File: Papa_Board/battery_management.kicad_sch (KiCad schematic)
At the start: 51 parts, among them J1 Conn_01x02_Female, J10 Conn_01x02_Female, J11 GND TEST CONN, J12 VOLTAGE TEST CONN, J7 Conn_01x02_Female, J9 Conn_01x02_Female, U1 INA180A4QDBVRQ1, U2 INA180A4QDBVRQ1, U3 LM22678TJ-5.0, U4 LDK320ADU120R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

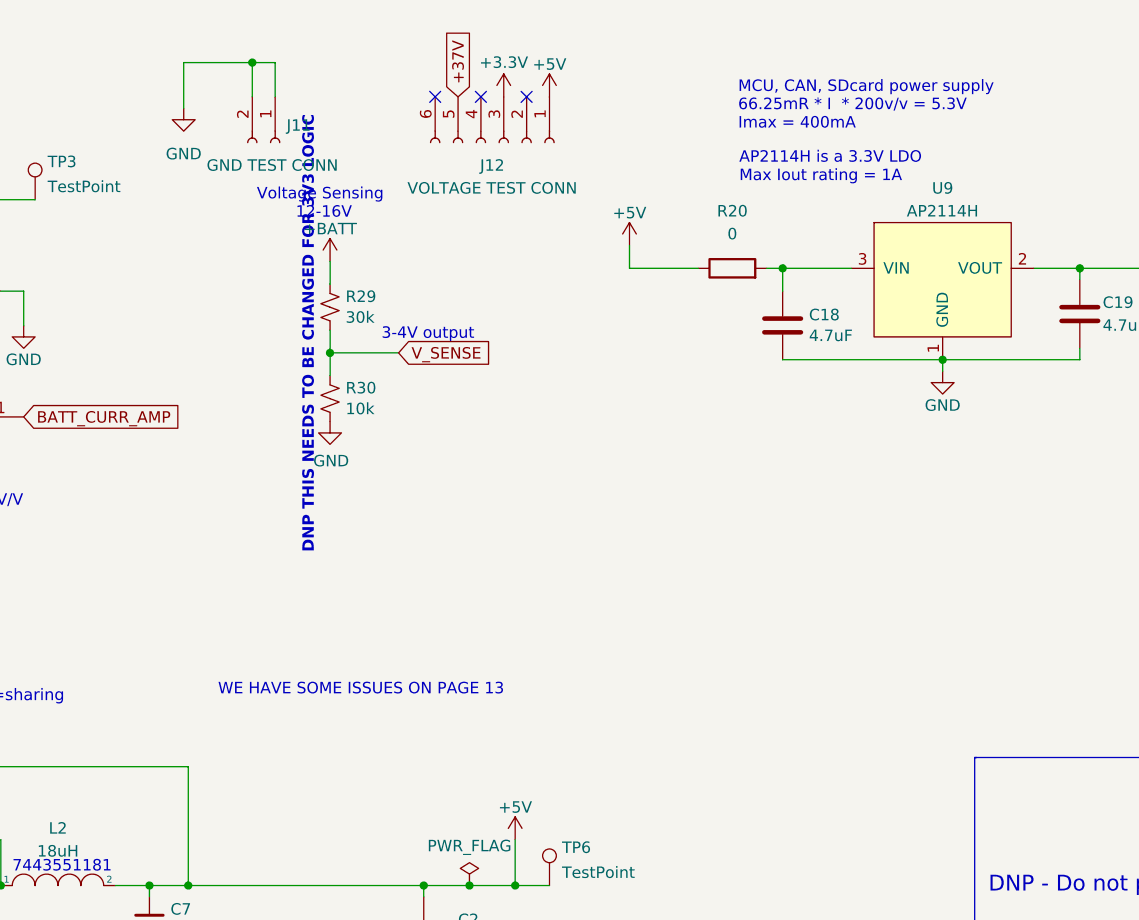
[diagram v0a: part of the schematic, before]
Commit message: Fix voltage sensing logic, finish lana's layout changes
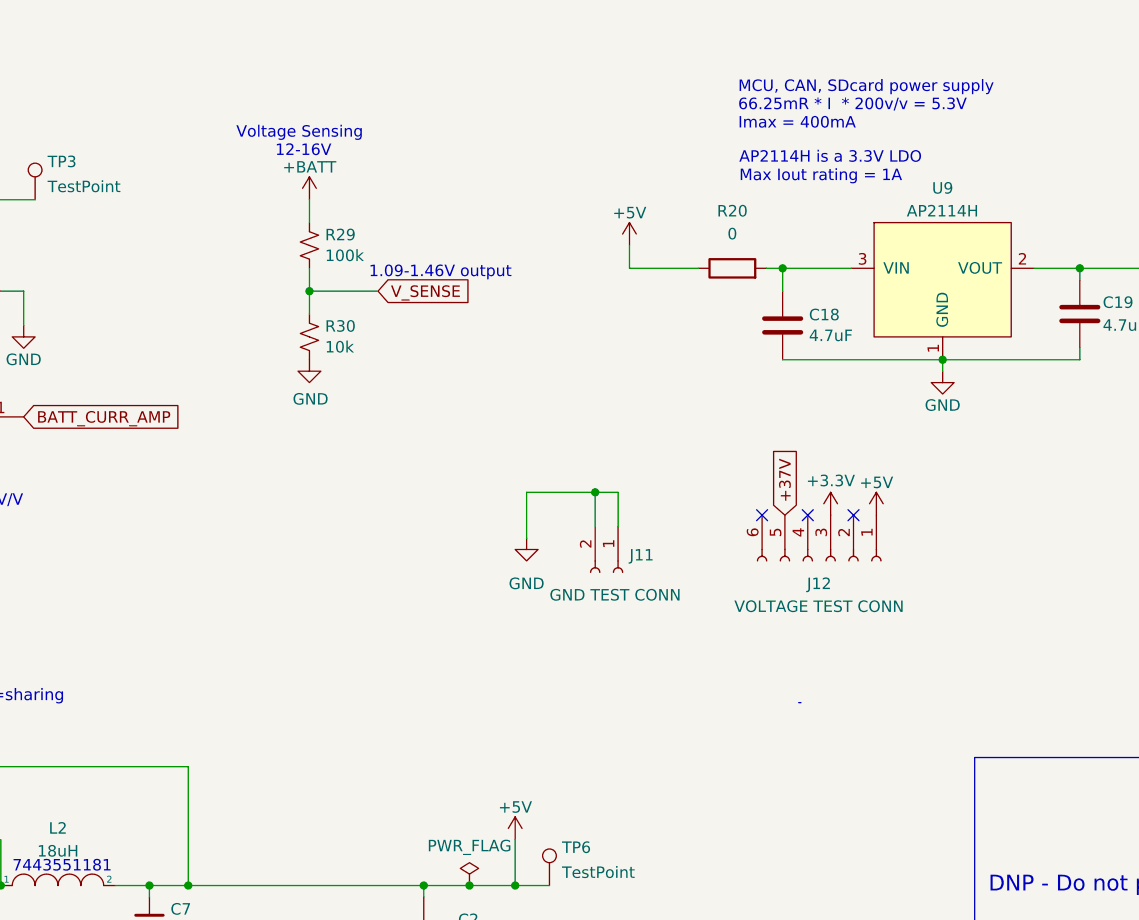
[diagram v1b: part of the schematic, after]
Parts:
- R29: value 30k -> 100k
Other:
- note added: "1.09-1.46V output"
- note removed: "3-4V output"
- note removed: "DNP THIS NEEDS TO BE CHANGED FOR 3V3 LOGIC"
- note removed: "WE HAVE SOME ISSUES ON PAGE 13"
- moved on the sheet: J11, J12, R29, R30

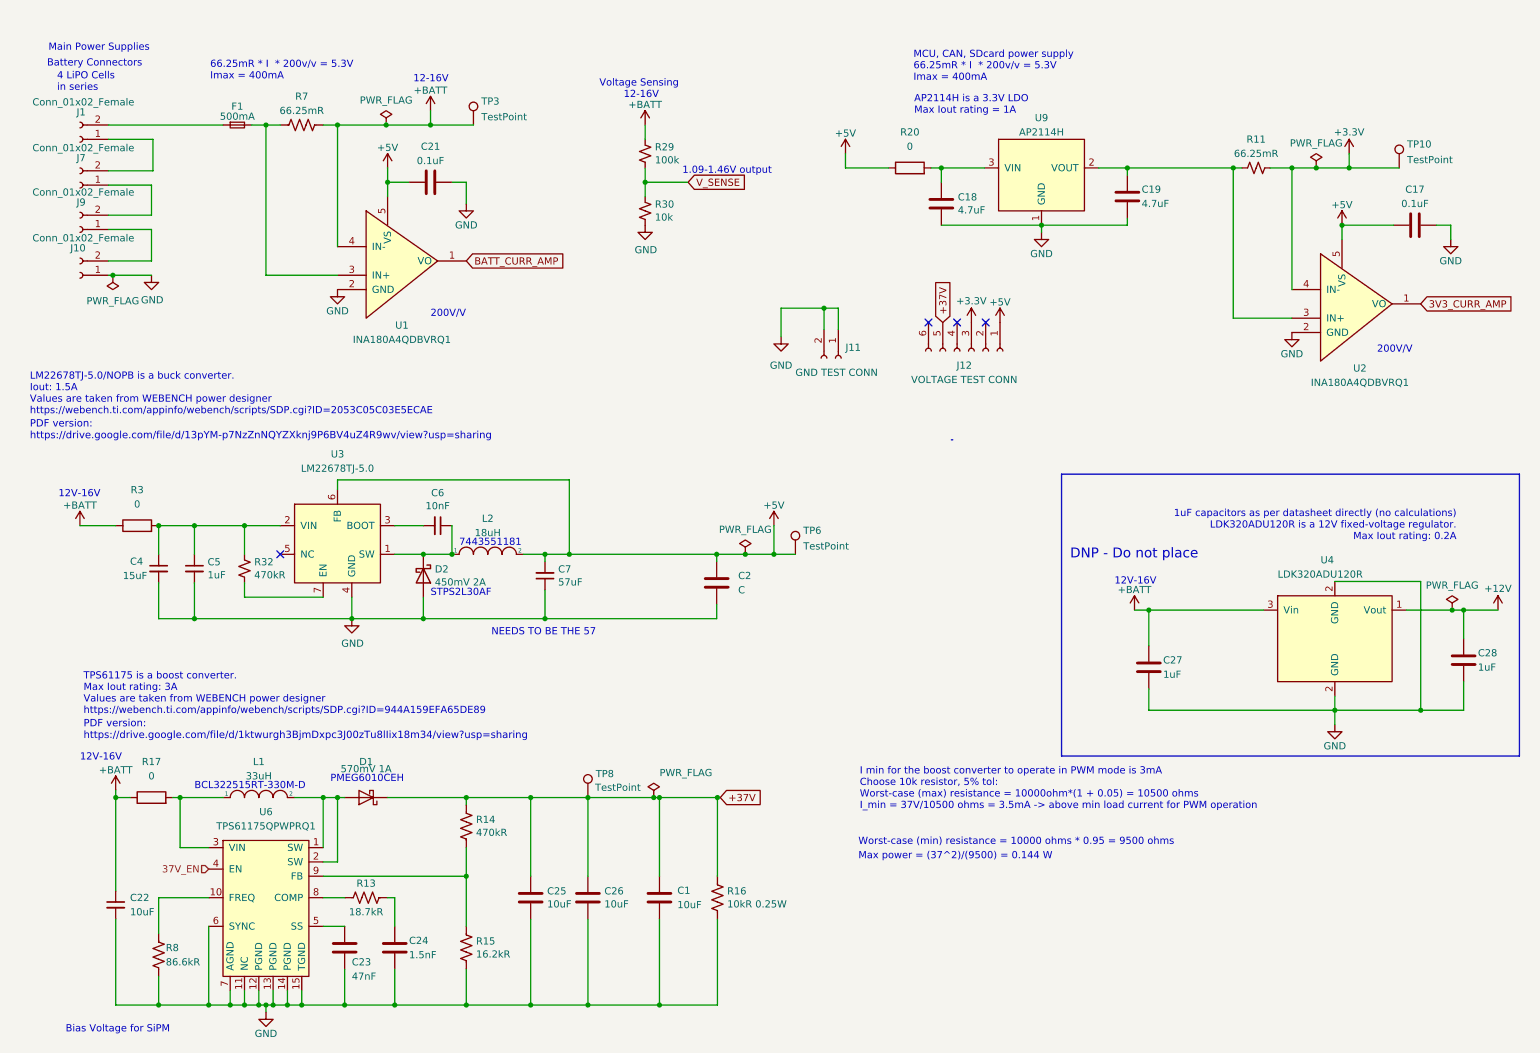
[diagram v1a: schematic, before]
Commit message: Address Jack's schematic review, still need to update PCB layout and figure out CAN connections
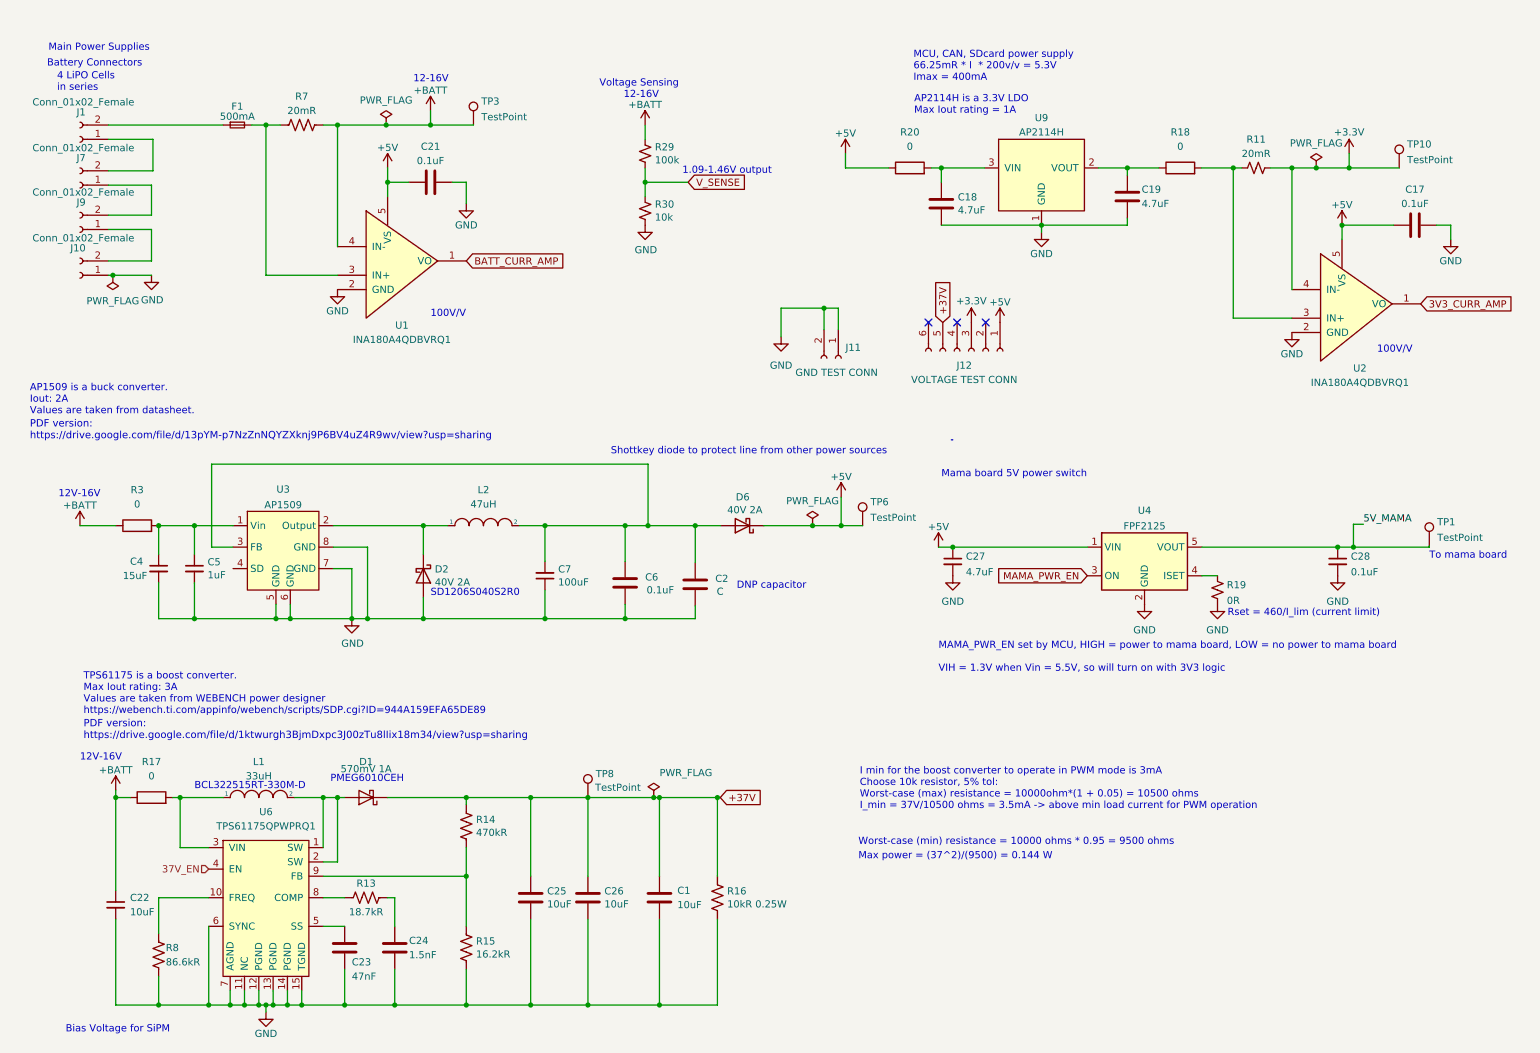
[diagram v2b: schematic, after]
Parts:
- removed C27, C28: 1uF, Capacitor_SMD:C_0805_2012Metric_Pad1.18x1.45mm_HandSolder, symbol Device:C
- removed C6: 10nF, Capacitor_SMD:C_0805_2012Metric_Pad1.18x1.45mm_HandSolder, symbol Device:C_Small
- removed R32: 470kR, Resistor_SMD:R_0805_2012Metric_Pad1.20x1.40mm_HandSolder, symbol Device:R_Small_US
- removed U3: LM22678TJ-5.0, Package_TO_SOT_SMD:TO-263-7_TabPin4, symbol payload2020_custom:LM22678TJ-5.0
- removed U4: LDK320ADU120R, Package_TO_SOT_SMD:SOT-89-3_Handsoldering, symbol payload2020_custom:LDK320ADU120R
- added C27: 4.7uF, Capacitor_SMD:C_0805_2012Metric_Pad1.18x1.45mm_HandSolder, symbol Device:C_Small
- added C28: 0.1uF, Capacitor_SMD:C_0805_2012Metric_Pad1.18x1.45mm_HandSolder, symbol Device:C_Small
- added C6: 0.1uF, Capacitor_SMD:C_0805_2012Metric_Pad1.18x1.45mm_HandSolder, symbol Device:C
- added D6: 40V 2A, Diode_SMD:D_1206_3216Metric_Pad1.42x1.75mm_HandSolder, symbol Device:D_Schottky
- added R18: 0, Resistor_SMD:R_0805_2012Metric_Pad1.20x1.40mm_HandSolder, symbol Device:R
- added R19: 0R, Resistor_SMD:R_0805_2012Metric_Pad1.20x1.40mm_HandSolder, symbol Device:R_Small_US
- added TP1: TestPoint, Connector_PinHeader_2.54mm:PinHeader_1x01_P2.54mm_Vertical, symbol Connector:TestPoint
- added U3: AP1509, symbol payload2020_custom:AP1509
- added U4: FPF2125, Package_TO_SOT_SMD:SOT-23-5_HandSoldering, symbol payload2020_custom:FPF2515
- C7: value 57uF -> 100uF; footprint Capacitor_SMD:C_1206_3216Metric_Pad1.42x1.75mm_HandSolder -> Capacitor_SMD:C_1206_3216Metric_Pad1.33x1.80mm_HandSolder
- D2: value 450mV 2A -> 40V 2A; footprint Diode_SMD:D_SMA_Handsoldering -> Diode_SMD:D_1206_3216Metric_Pad1.42x1.75mm_HandSolder
- L2: value 18uH -> 47uH
- R11, R7: value 66.25mR -> 20mR
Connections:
- net +5V: now also C27.1, D6.1 (K), U4.1 (VIN); no longer C2.1, C7.2, L2.2
- net GND: now also C27.2, C28.2, C6.2, R19.2, U3.5 (GND), U3.6 (GND), U3.7 (GND), U3.8 (GND), U4.2 (GND)
- net at R11.2, U2.3 (IN+): now also R18.2; no longer C19.2, U9.2 (VOUT)
- net at D2.1 (K), L2.1: now also U3.2 (Output)
- net at C4.1, C5.1, R3.2: now also U3.1 (Vin)
- new net: C19.2, R18.1, U9.2 (VOUT)
- new net: C2.1, C6.1, C7.2, D6.2 (A), L2.2, U3.3 (FB)
- new net: R19.1, U4.4 (ISET)
- new net 5V_MAMA: C28.1, TP1.1, U4.5 (VOUT)
- new net MAMA_PWR_EN: U4.3 (ON)
- no-connect marks 4 -> 3
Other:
- note added: "100V/V"
- note added: "AP1509 is a buck converter. Iout: 2A Values are taken from datasheet."
- note added: "DNP capacitor"
- note added: "MAMA_PWR_EN set by MCU, HIGH = power to mama board, LOW = no power to mama board"
- note added: "Mama board 5V power switch"
- note added: "Rset = 460/I_lim (current limit)"
- note added: "SD1206S040S2R0"
- note added: "Shottkey diode to protect line from other power sources"
- note added: "To mama board"
- note added: "VIH = 1.3V when Vin = 5.5V, so will turn on with 3V3 logic"
- note removed: "1uF capacitors as per datasheet directly (no calculations) LDK320ADU120R is a 12V fixed-voltage regulator. Max Iout rating: 0.2A"
- note removed: "200V/V"
- note removed: "7443551181"
- note removed: "DNP - Do not place"
- note removed: "LM22678TJ-5.0/NOPB is a buck converter. Iout: 1.5A Values are taken from WEBENCH power designer https://webench.ti.com/appinfo/webench/scripts/SDP.cgi?ID=2053C05C03E5ECAE"
- note removed: "NEEDS TO BE THE 57"
- note removed: "STPS2L30AF"
- moved on the sheet: C2, L2, TP6

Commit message: Finish PCB layout updates
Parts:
- L2: footprint Inductor_SMD:L_Wuerth_HCI-1365 -> Inductor_THT:L_Radial_D8.7mm_P5.00mm_Fastron_07HCP
- U3: footprint (none) -> Package_SO:SOIC-8_3.9x4.9mm_P1.27mm
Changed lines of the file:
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@@
-    (stroke (width 0) (type default) (color 0 0 0 0))
-  )
-  (wire (pts (xy 250.19 103.886) (xy 251.968 103.886))
     (stroke (width 0) (type default) (color 0 0 0 0))
   )
@@
     (effects (font (size 1.27 1.27)) (justify left bottom))
   )
-  (label "5V_MAMA" (at 251.968 103.886 0)
-    (effects (font (size 1.27 1.27)) (justify left bottom))
-  )
   (global_label "+37V" (shape input) (at 137.795 152.4 0) (fields_autoplaced)
     (effects (font (size 1.27 1.27)) (justify left))
     (property "Intersheet References" "${INTERSHEET_REFS}" (id 0) (at 145.1992 152.3206 0)
+      (effects (font (size 1.27 1.27)) (justify left) hide)
+    )
+  )
+  (global_label "5V_MAMA" (shape input) (at 250.19 103.886 0) (fields_autoplaced)
+    (effects (font (size 1.27 1.27)) (justify left))
+    (property "Intersheet References" "${INTERSHEET_REFS}" (id 0) (at 260.8599 103.8066 0)
       (effects (font (size 1.27 1.27)) (justify left) hide)
     )
@@
     (property "Reference" "L2" (id 0) (at 95.758 97.79 0))
     (property "Value" "47uH" (id 1) (at 95.758 100.33 0))
-    (property "Footprint" "Inductor_SMD:L_Wuerth_HCI-1365" (id 2) (at 95.758 104.14 0)
+    (property "Footprint" "Inductor_THT:L_Radial_D8.7mm_P5.00mm_Fastron_07HCP" (id 2) (at 95.758 104.14 0)
       (effects (font (size 1.27 1.27)) hide)
     )
@@
     (property "Reference" "U3" (id 0) (at 60.198 97.6843 0))
     (property "Value" "AP1509" (id 1) (at 60.198 100.4594 0))
-    (property "Footprint" "" (id 2) (at 60.198 107.95 0)
-      (effects (font (size 1.27 1.27)) hide)
-    )
+    (property "Footprint" "Package_SO:SOIC-8_3.9x4.9mm_P1.27mm" (id 2) (at 60.198 107.95 0)
+      (effects (font (size 1.27 1.27)) hide)
+    )

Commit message: Add logger board connector, CAN lines to mama board
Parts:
- removed J12: VOLTAGE TEST CONN, Connector_PinHeader_2.54mm:PinHeader_1x06_P2.54mm_Vertical, symbol Connector:Conn_01x06_Female
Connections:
- no-connect marks 3 -> 0
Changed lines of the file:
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@@
   (junction (at 55.88 189.23) (diameter 0) (color 0 0 0 0)
   )
-  (no_connect (at 179.832 68.072))
-  (no_connect (at 174.752 68.072))
-  (no_connect (at 184.912 68.072))
   (wire (pts (xy 75.184 107.95) (xy 75.184 120.65))
     (stroke (width 0) (type default) (color 0 0 0 0))
@@
     (property "Intersheet References" "${INTERSHEET_REFS}" (id 0) (at 80.518 0 0)
       (effects (font (size 1.27 1.27)) hide)
-    )
-  )
-  (global_label "+37V" (shape input) (at 177.292 68.072 90) (fields_autoplaced)
-    (effects (font (size 1.27 1.27)) (justify left))
-    (property "Intersheet References" "${INTERSHEET_REFS}" (id 0) (at 177.2126 60.6678 90)
-      (effects (font (size 1.27 1.27)) (justify left) hide)
     )
   )
@@
     (pin "1")
   )
-  (symbol (lib_id "Connector:Conn_01x06_Female") (at 182.372 73.152 270) (unit 1)
-    (in_bom yes) (on_board yes) (fields_autoplaced)
-    (property "Reference" "J12" (id 0) (at 181.102 75.692 90))
-    (property "Value" "VOLTAGE TEST CONN" (id 1) (at 181.102 78.232 90))
-    (property "Footprint" "Connector_PinHeader_2.54mm:PinHeader_1x06_P2.54mm_Vertical" (id 2) (at 182.372 73.152 0)
-      (effects (font (size 1.27 1.27)) hide)
-    )
-    (property "Datasheet" "~" (id 3) (at 182.372 73.152 0)
-      (effects (font (size 1.27 1.27)) hide)
-    )
-    (pin "1")
-    (pin "2")
-    (pin "3")
-    (pin "4")
-    (pin "5")
-    (pin "6")
-  )
   (symbol (lib_id "Connector:TestPoint") (at 258.318 40.64 0) (unit 1)
     (in_bom yes) (on_board yes) (fields_autoplaced)
@@
     (pin "2")
   )
-  (symbol (lib_id "power:+5V") (at 187.452 68.072 0) (unit 1)
-    (in_bom yes) (on_board yes) (fields_autoplaced)
-    (property "Reference" "#PWR021" (id 0) (at 187.452 71.882 0)
-      (effects (font (size 1.27 1.27)) hide)
-    )
-    (property "Value" "+5V" (id 1) (at 187.452 64.4675 0))
-    (property "Footprint" "" (id 2) (at 187.452 68.072 0)
-      (effects (font (size 1.27 1.27)) hide)
-    )
-    (property "Datasheet" "" (id 3) (at 187.452 68.072 0)
-      (effects (font (size 1.27 1.27)) hide)
-    )
-    (pin "1")
-  )
-  (symbol (lib_id "power:+3.3V") (at 182.372 68.072 0) (unit 1)
-    (in_bom yes) (on_board yes)
-    (property "Reference" "#PWR017" (id 0) (at 182.372 71.882 0)
-      (effects (font (size 1.27 1.27)) hide)
-    )
-    (property "Value" "+3.3V" (id 1) (at 182.372 64.262 0))
-    (property "Footprint" "" (id 2) (at 182.372 68.072 0)
-      (effects (font (size 1.27 1.27)) hide)
-    )
-    (property "Datasheet" "" (id 3) (at 182.372 68.072 0)
-      (effects (font (size 1.27 1.27)) hide)
-    )
-    (pin "1")
-  )
 )

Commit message: grounded sd pin
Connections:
- net GND: now also U3.4 (SD)
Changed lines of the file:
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@@
   (junction (at 78.74 43.18) (diameter 0) (color 0 0 0 0)
   )
+  (junction (at 51.308 111.76) (diameter 0) (color 0 0 0 0)
+  )
   (junction (at 58.42 189.23) (diameter 0) (color 0 0 0 0)
   )
@@
   (junction (at 44.45 104.14) (diameter 0) (color 0 0 0 0)
   )
+  (junction (at 50.8 120.65) (diameter 0) (color 0 0 0 0)
+  )
   (junction (at 92.71 152.4) (diameter 0) (color 0 0 0 0)
   )
@@
     (stroke (width 0) (type default) (color 0 0 0 0))
   )
-  (wire (pts (xy 44.45 120.65) (xy 58.928 120.65))
+  (wire (pts (xy 50.8 111.76) (xy 50.8 120.65))
+    (stroke (width 0) (type default) (color 0 0 0 0))
+  )
+  (wire (pts (xy 44.45 120.65) (xy 50.8 120.65))
     (stroke (width 0) (type default) (color 0 0 0 0))
   )
@@
     (stroke (width 0) (type default) (color 0 0 0 0))
   )
+  (wire (pts (xy 51.435 111.76) (xy 51.308 111.76))
+    (stroke (width 0) (type default) (color 0 0 0 0))
+  )
   (wire (pts (xy 78.74 40.64) (xy 78.74 43.18))
     (stroke (width 0) (type default) (color 0 0 0 0))
@@
     (stroke (width 0) (type default) (color 0 0 0 0))
   )
+  (wire (pts (xy 50.8 120.65) (xy 58.928 120.65))
+    (stroke (width 0) (type default) (color 0 0 0 0))
+  )
   (wire (pts (xy 69.85 33.02) (xy 78.486 33.02))
     (stroke (width 0) (type default) (color 0 0 0 0))
@@
     (stroke (width 0) (type default) (color 0 0 0 0))
   )
+  (wire (pts (xy 51.308 111.76) (xy 50.8 111.76))
+    (stroke (width 0) (type default) (color 0 0 0 0))
+  )
